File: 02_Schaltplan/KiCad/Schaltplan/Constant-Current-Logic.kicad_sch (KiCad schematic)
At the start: 42 parts, among them Q1 SI2318, U17 LMV321AUIDBVR, U18 LMV358MM, U19 INA826AIDRGT, U20 74HC595, U21 74HC595, U22 74AHC2G08

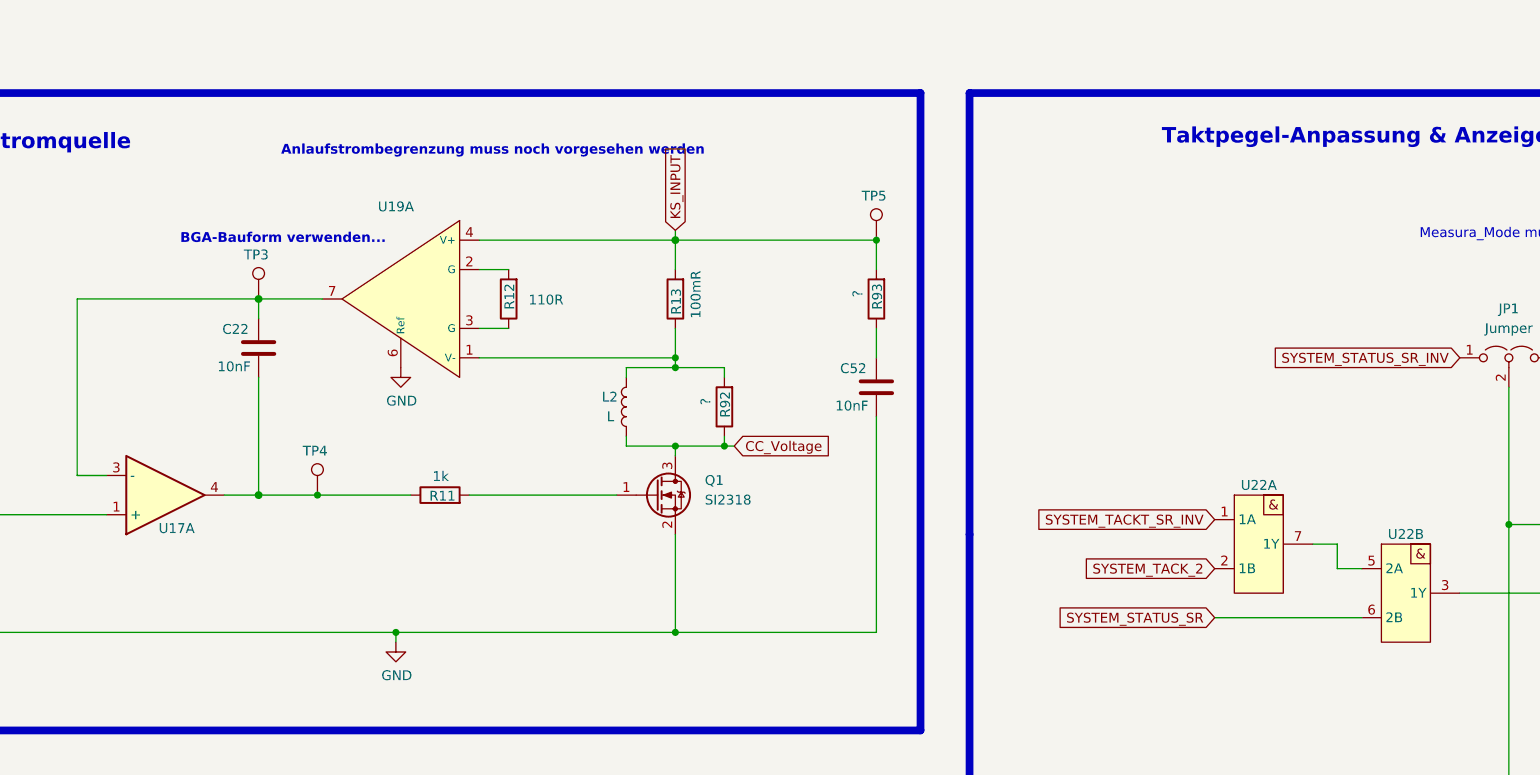
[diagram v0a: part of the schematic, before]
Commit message: Changes
constant-current
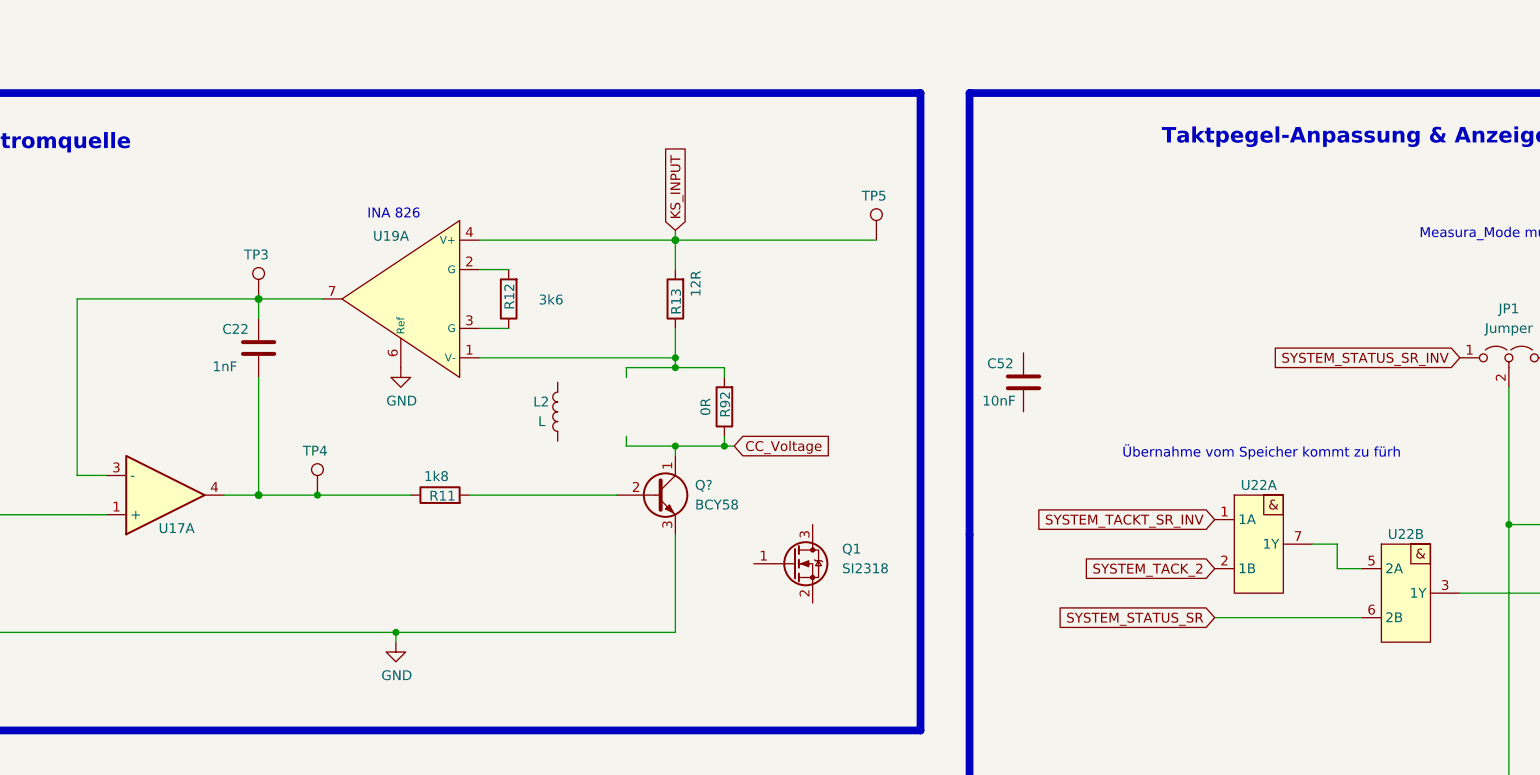
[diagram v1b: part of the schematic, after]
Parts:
- removed R93: ?, Resistor_SMD:R_0603_1608Metric_Pad0.98x0.95mm_HandSolder, symbol Device:R
- added Q?: BCY58, Package_TO_SOT_THT:TO-92_Inline, symbol Transistor_BJT:BC413
- C22: value 10nF -> 1nF
- R11: value 1k -> 1k8
- R12: value 110R -> 3k6
- R13: value 100mR -> 12R
- R92: value ? -> 0R
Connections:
- net CC_Voltage: now also Q?.1 (C); no longer L2.2, Q1.3 (D)
- net GND: now also Q?.3 (E); no longer C52.2, Q1.2 (S)
- net at R13.1, R92.2, U19.1 (V-): no longer L2.1
- net at R11.2: now also Q?.2 (B); no longer Q1.1 (G)
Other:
- note added: "INA 826"
- note added: "Übernahme vom Speicher kommt zu fürh"
- note removed: "Anlaufstrombegrenzung muss noch vorgesehen werden"
- note removed: "BGA-Bauform verwenden..."
- moved on the sheet: C52, L2, Q1
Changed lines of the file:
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@@
   (junction (at 171.45 86.36) (diameter 0.9144) (color 0 0 0 0))
   (junction (at 171.45 96.52) (diameter 0.9144) (color 0 0 0 0))
-  (junction (at 171.45 120.65) (diameter 0.9144) (color 0 0 0 0))
   (junction (at 174.625 243.84) (diameter 1.016) (color 0 0 0 0))
   (junction (at 174.625 265.43) (diameter 1.016) (color 0 0 0 0))
   (junction (at 177.8 96.52) (diameter 0.9144) (color 0 0 0 0))
-  (junction (at 197.485 69.85) (diameter 0.9144) (color 0 0 0 0))
   (junction (at 250.825 243.84) (diameter 0.9144) (color 0 0 0 0))
   (junction (at 250.825 264.16) (diameter 0.9144) (color 0 0 0 0))
@@
     (stroke (width 0) (type solid) (color 0 0 0 0))
   )
-  (wire (pts (xy 197.485 69.85) (xy 197.485 73.66))
-    (stroke (width 0) (type solid) (color 0 0 0 0))
-  )
-  (wire (pts (xy 197.485 81.28) (xy 197.485 85.09))
-    (stroke (width 0) (type solid) (color 0 0 0 0))
-  )
-  (wire (pts (xy 197.485 92.71) (xy 197.485 120.65))
-    (stroke (width 0) (type solid) (color 0 0 0 0))
-  )
-  (wire (pts (xy 197.485 120.65) (xy 171.45 120.65))
-    (stroke (width 0) (type solid) (color 0 0 0 0))
-  )
   (wire (pts (xy 241.3 118.745) (xy 260.35 118.745))
     (stroke (width 0) (type solid) (color 0 0 0 0))
@@
     (effects (font (size 2 2) (thickness 0.4) bold) (justify right bottom))
   )
-  (text "BGA-Bauform verwenden...\n" (at 133.985 70.485 180)
-    (effects (font (size 1.27 1.27) (thickness 0.254) bold) (justify right bottom))
-  )
-  (text "Anlaufstrombegrenzung muss noch vorgesehen werden\n"
-    (at 175.26 59.055 0)
-    (effects (font (size 1.27 1.27) (thickness 0.254) bold) (justify right bottom))
+  (text "INA 826\n" (at 138.43 67.31 180)
+    (effects (font (size 1.27 1.27)) (justify right bottom))
   )
   (text "Hysterese-Widerstand\n" (at 178.435 168.275 180)
+    (effects (font (size 1.27 1.27)) (justify right bottom))
+  )
+  (text "Übernahme vom Speicher kommt zu fürh\n\n" (at 265.43 100.33 180)
     (effects (font (size 1.27 1.27)) (justify right bottom))
   )
@@
     (pin "1")
   )
-  (symbol (lib_id "Device:L") (at 165.1 91.44 0) (mirror y) (unit 1)
-    (in_bom yes) (on_board yes)
-    (property "Reference" "L2" (id 0) (at 161.925 90.17 0)
+  (symbol (lib_id "Device:L") (at 156.21 92.075 0) (mirror y) (unit 1)
+    (in_bom yes) (on_board yes)
+    (property "Reference" "L2" (id 0) (at 153.035 90.805 0)
       (effects (font (size 1.27 1.27)) (justify right))
     )
-    (property "Value" "L" (id 1) (at 162.56 92.71 0)
+    (property "Value" "L" (id 1) (at 153.67 93.345 0)
       (effects (font (size 1.27 1.27)) (justify right))
     )
-    (property "Footprint" "Inductor_SMD:L_TDK_NLV32_3.2x2.5mm" (id 2) (at 165.1 91.44 0)
-      (effects (font (size 1.27 1.27)) hide)
-    )
-    (property "Datasheet" "~" (id 3) (at 165.1 91.44 0)
+    (property "Footprint" "Inductor_SMD:L_TDK_NLV32_3.2x2.5mm" (id 2) (at 156.21 92.075 0)
+      (effects (font (size 1.27 1.27)) hide)
+    )
+    (property "Datasheet" "~" (id 3) (at 156.21 92.075 0)
       (effects (font (size 1.27 1.27)) hide)
     )
@@
       (effects (font (size 1.27 1.27)) (justify left))
     )
-    (property "Value" "1k" (id 1) (at 142.119 100.457 90)
+    (property "Value" "1k8" (id 1) (at 142.119 100.457 90)
       (effects (font (size 1.27 1.27)) (justify left))
     )
@@
       (effects (font (size 1.27 1.27)) (justify left))
     )
-    (property "Value" "110R" (id 1) (at 156.972 77.591 0)
+    (property "Value" "3k6" (id 1) (at 156.972 77.591 0)
       (effects (font (size 1.27 1.27)) (justify left))
     )
@@
       (effects (font (size 1.27 1.27)) (justify left))
     )
-    (property "Value" "100mR" (id 1) (at 174.117 73.781 90)
+    (property "Value" "12R" (id 1) (at 174.117 73.781 90)
       (effects (font (size 1.27 1.27)) (justify left))
     )
@@
       (effects (font (size 1.27 1.27)) (justify left))
     )
-    (property "Value" "?" (id 1) (at 175.387 90.291 90)
+    (property "Value" "0R" (id 1) (at 175.387 90.291 90)
       (effects (font (size 1.27 1.27)) (justify left))
     )
@@
     (pin "2")
   )
-  (symbol (lib_id "Device:R") (at 197.485 77.47 180) (unit 1)
-    (in_bom yes) (on_board yes)
-    (property "Reference" "R93" (id 0) (at 197.6119 75.4444 90)
-      (effects (font (size 1.27 1.27)) (justify left))
-    )
-    (property "Value" "?" (id 1) (at 195.072 76.321 90)
-      (effects (font (size 1.27 1.27)) (justify left))
-    )
-    (property "Footprint" "Resistor_SMD:R_0603_1608Metric_Pad0.98x0.95mm_HandSolder" (id 2) (at 199.263 77.47 90)
-      (effects (font (size 1.27 1.27)) hide)
-    )
-    (property "Datasheet" "~" (id 3) (at 197.485 77.47 0)
-      (effects (font (size 1.27 1.27)) hide)
-    )
-    (property "BMK-Nr" "BS" (id 4) (at 197.485 77.47 0)
-      (effects (font (size 1.27 1.27)) hide)
-    )
-    (property "Mouser" "-" (id 4) (at 197.485 77.47 0)
-      (effects (font (size 1.27 1.27)) hide)
-    )
-    (pin "1")
-    (pin "2")
-  )
   (symbol (lib_name "Device:C_2") (lib_id "Device:C") (at 82.55 254 0) (unit 1)
     (in_bom yes) (on_board yes)
@@
       (effects (font (size 1.27 1.27)) (justify left))
     )
-    (property "Value" "10nF" (id 1) (at 112.141 86.239 0)
+    (property "Value" "1nF" (id 1) (at 111.506 86.239 0)
       (effects (font (size 1.27 1.27)) (justify left))
     )
@@
     (pin "2")
   )
-  (symbol (lib_name "Device:C_6") (lib_id "Device:C") (at 197.485 88.9 0) (unit 1)
-    (in_bom yes) (on_board yes)
-    (property "Reference" "C52" (id 0) (at 192.7861 86.4806 0)
-      (effects (font (size 1.27 1.27)) (justify left))
-    )
-    (property "Value" "10nF" (id 1) (at 192.151 91.319 0)
-      (effects (font (size 1.27 1.27)) (justify left))
-    )
-    (property "Footprint" "Capacitor_SMD:C_0603_1608Metric_Pad1.08x0.95mm_HandSolder" (id 2) (at 198.4502 92.71 0)
-      (effects (font (size 1.27 1.27)) hide)
-    )
-    (property "Datasheet" "~" (id 3) (at 197.485 88.9 0)
-      (effects (font (size 1.27 1.27)) hide)
-    )
-    (property "BMK-Nr" "BS" (id 4) (at 197.485 88.9 0)
+  (symbol (lib_name "Device:C_6") (lib_id "Device:C") (at 216.535 88.265 0) (unit 1)
+    (in_bom yes) (on_board yes)
+    (property "Reference" "C52" (id 0) (at 211.8361 85.8456 0)
+      (effects (font (size 1.27 1.27)) (justify left))
+    )
+    (property "Value" "10nF" (id 1) (at 211.201 90.684 0)
+      (effects (font (size 1.27 1.27)) (justify left))
+    )
+    (property "Footprint" "Capacitor_SMD:C_0603_1608Metric_Pad1.08x0.95mm_HandSolder" (id 2) (at 217.5002 92.075 0)
+      (effects (font (size 1.27 1.27)) hide)
+    )
+    (property "Datasheet" "~" (id 3) (at 216.535 88.265 0)
+      (effects (font (size 1.27 1.27)) hide)
+    )
+    (property "BMK-Nr" "BS" (id 4) (at 216.535 88.265 0)
       (effects (font (size 1.27 1.27)) hide)
     )
@@
     (pin "3")
   )
-  (symbol (lib_id "Transistor_FET:BSS123") (at 168.91 102.87 0) (unit 1)
-    (in_bom yes) (on_board yes)
-    (property "Reference" "Q1" (id 0) (at 175.26 100.965 0)
-      (effects (font (size 1.27 1.27)) (justify left))
-    )
-    (property "Value" "SI2318" (id 1) (at 175.26 103.505 0)
-      (effects (font (size 1.27 1.27)) (justify left))
-    )
-    (property "Footprint" "Package_TO_SOT_SMD:SOT-23" (id 2) (at 173.99 104.775 0)
+  (symbol (lib_id "Transistor_BJT:BC413") (at 168.91 102.87 0) (unit 1)
+    (in_bom yes) (on_board yes)
+    (property "Reference" "Q?" (id 0) (at 173.99 101.6 0)
+      (effects (font (size 1.27 1.27)) (justify left))
+    )
+    (property "Value" "BCY58" (id 1) (at 173.99 104.14 0)
+      (effects (font (size 1.27 1.27)) (justify left))
+    )
+    (property "Footprint" "Package_TO_SOT_THT:TO-92_Inline" (id 2) (at 173.99 104.775 0)
       (effects (font (size 1.27 1.27) italic) (justify left) hide)
     )
-    (property "Datasheet" "http://www.diodes.com/assets/Datasheets/ds30366.pdf" (id 3) (at 168.91 102.87 0)
-      (effects (font (size 1.27 1.27)) (justify left) hide)
-    )
-    (property "BMK-Nr" "08-8668" (id 4) (at 168.91 102.87 0)
-      (effects (font (size 1.27 1.27)) hide)
-    )
-    (property "Mouser" "781-SI2318CDS-T1-GE3" (id 4) (at 168.91 102.87 0)
+    (property "Datasheet" "http://www.cdil.com/datasheets/bc413_14_b_c.pdf" (id 3) (at 168.91 102.87 0)
+      (effects (font (size 1.27 1.27)) (justify left) hide)
+    )
+    (pin "1")
+    (pin "2")
+    (pin "3")
+  )
+  (symbol (lib_id "Transistor_FET:BSS123") (at 186.69 111.76 0) (unit 1)
+    (in_bom yes) (on_board yes)
+    (property "Reference" "Q1" (id 0) (at 193.04 109.855 0)
+      (effects (font (size 1.27 1.27)) (justify left))
+    )
+    (property "Value" "SI2318" (id 1) (at 193.04 112.395 0)
+      (effects (font (size 1.27 1.27)) (justify left))
+    )
+    (property "Footprint" "Package_TO_SOT_SMD:SOT-23" (id 2) (at 191.77 113.665 0)
+      (effects (font (size 1.27 1.27) italic) (justify left) hide)
+    )
+    (property "Datasheet" "http://www.diodes.com/assets/Datasheets/ds30366.pdf" (id 3) (at 186.69 111.76 0)
+      (effects (font (size 1.27 1.27)) (justify left) hide)
+    )
+    (property "BMK-Nr" "08-8668" (id 4) (at 186.69 111.76 0)
+      (effects (font (size 1.27 1.27)) hide)
+    )
+    (property "Mouser" "781-SI2318CDS-T1-GE3" (id 4) (at 186.69 111.76 0)
       (effects (font (size 1.27 1.27)) hide)
     )
@@
   (symbol (lib_id "Kabeltester:INA826AIDRGT") (at 137.795 77.47 0) (mirror y) (unit 1)
     (in_bom yes) (on_board yes)
-    (property "Reference" "U19" (id 0) (at 135.255 65.5256 0))
+    (property "Reference" "U19" (id 0) (at 134.62 69.3356 0))
     (property "Value" "INA826AIDRGT" (id 1) (at 134.62 67.672 0)
       (effects (font (size 1.27 1.27)) hide)

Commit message: Changes
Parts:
- removed C52: 10nF, Capacitor_SMD:C_0603_1608Metric_Pad1.08x0.95mm_HandSolder, symbol Device:C
- removed Q?: BCY58, Package_TO_SOT_THT:TO-92_Inline, symbol Transistor_BJT:BC413
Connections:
- net CC_Voltage: now also L2.2, Q1.3 (D)
- net GND: now also Q1.2 (S)
- net at R11.2: now also Q1.1 (G)
- net at R13.1, R92.2, U19.1 (V-): now also L2.1
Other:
- note added: "Übernahme vom Speicher kommt zu fürh Takt2 inv"
- note removed: "Übernahme vom Speicher kommt zu fürh"
- moved on the sheet: L2, Q1
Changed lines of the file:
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@@
     (stroke (width 1) (type solid) (color 255 0 0 1))
+  )
+  (polyline (pts (xy 167.64 88.9) (xy 161.925 94.615))
+    (stroke (width 0.3) (type solid) (color 255 0 0 1))
+  )
+  (polyline (pts (xy 167.64 94.615) (xy 161.925 88.9))
+    (stroke (width 0.3) (type solid) (color 255 0 0 1))
   )
   (polyline (pts (xy 203.2 50.8) (xy 203.2 133.35))
@@
     (effects (font (size 1.27 1.27)) (justify right bottom))
   )
-  (text "Übernahme vom Speicher kommt zu fürh\n\n" (at 265.43 100.33 180)
+  (text "Übernahme vom Speicher kommt zu fürh\n\nTakt2 inv\n" (at 265.43 100.33 180)
     (effects (font (size 1.27 1.27)) (justify right bottom))
   )
@@
     (pin "1")
   )
-  (symbol (lib_id "Device:L") (at 156.21 92.075 0) (mirror y) (unit 1)
-    (in_bom yes) (on_board yes)
-    (property "Reference" "L2" (id 0) (at 153.035 90.805 0)
+  (symbol (lib_id "Device:L") (at 165.1 91.44 0) (mirror y) (unit 1)
+    (in_bom yes) (on_board yes)
+    (property "Reference" "L2" (id 0) (at 161.925 90.17 0)
       (effects (font (size 1.27 1.27)) (justify right))
     )
-    (property "Value" "L" (id 1) (at 153.67 93.345 0)
+    (property "Value" "L" (id 1) (at 162.56 92.71 0)
       (effects (font (size 1.27 1.27)) (justify right))
     )
-    (property "Footprint" "Inductor_SMD:L_TDK_NLV32_3.2x2.5mm" (id 2) (at 156.21 92.075 0)
-      (effects (font (size 1.27 1.27)) hide)
-    )
-    (property "Datasheet" "~" (id 3) (at 156.21 92.075 0)
+    (property "Footprint" "Inductor_SMD:L_TDK_NLV32_3.2x2.5mm" (id 2) (at 165.1 91.44 0)
+      (effects (font (size 1.27 1.27)) hide)
+    )
+    (property "Datasheet" "~" (id 3) (at 165.1 91.44 0)
       (effects (font (size 1.27 1.27)) hide)
     )
@@
     )
     (property "BMK-Nr" "BS" (id 4) (at 184.15 254 0)
-      (effects (font (size 1.27 1.27)) hide)
-    )
-    (pin "1")
-    (pin "2")
-  )
-  (symbol (lib_name "Device:C_6") (lib_id "Device:C") (at 216.535 88.265 0) (unit 1)
-    (in_bom yes) (on_board yes)
-    (property "Reference" "C52" (id 0) (at 211.8361 85.8456 0)
-      (effects (font (size 1.27 1.27)) (justify left))
-    )
-    (property "Value" "10nF" (id 1) (at 211.201 90.684 0)
-      (effects (font (size 1.27 1.27)) (justify left))
-    )
-    (property "Footprint" "Capacitor_SMD:C_0603_1608Metric_Pad1.08x0.95mm_HandSolder" (id 2) (at 217.5002 92.075 0)
-      (effects (font (size 1.27 1.27)) hide)
-    )
-    (property "Datasheet" "~" (id 3) (at 216.535 88.265 0)
-      (effects (font (size 1.27 1.27)) hide)
-    )
-    (property "BMK-Nr" "BS" (id 4) (at 216.535 88.265 0)
       (effects (font (size 1.27 1.27)) hide)
     )
@@
     (pin "3")
   )
-  (symbol (lib_id "Transistor_BJT:BC413") (at 168.91 102.87 0) (unit 1)
-    (in_bom yes) (on_board yes)
-    (property "Reference" "Q?" (id 0) (at 173.99 101.6 0)
-      (effects (font (size 1.27 1.27)) (justify left))
-    )
-    (property "Value" "BCY58" (id 1) (at 173.99 104.14 0)
-      (effects (font (size 1.27 1.27)) (justify left))
-    )
-    (property "Footprint" "Package_TO_SOT_THT:TO-92_Inline" (id 2) (at 173.99 104.775 0)
+  (symbol (lib_id "Transistor_FET:BSS123") (at 168.91 102.87 0) (unit 1)
+    (in_bom yes) (on_board yes)
+    (property "Reference" "Q1" (id 0) (at 175.26 100.965 0)
+      (effects (font (size 1.27 1.27)) (justify left))
+    )
+    (property "Value" "SI2318" (id 1) (at 175.26 103.505 0)
+      (effects (font (size 1.27 1.27)) (justify left))
+    )
+    (property "Footprint" "Package_TO_SOT_SMD:SOT-23" (id 2) (at 173.99 104.775 0)
       (effects (font (size 1.27 1.27) italic) (justify left) hide)
     )
-    (property "Datasheet" "http://www.cdil.com/datasheets/bc413_14_b_c.pdf" (id 3) (at 168.91 102.87 0)
-      (effects (font (size 1.27 1.27)) (justify left) hide)
-    )
-    (pin "1")
-    (pin "2")
-    (pin "3")
-  )
-  (symbol (lib_id "Transistor_FET:BSS123") (at 186.69 111.76 0) (unit 1)
-    (in_bom yes) (on_board yes)
-    (property "Reference" "Q1" (id 0) (at 193.04 109.855 0)
-      (effects (font (size 1.27 1.27)) (justify left))
-    )
-    (property "Value" "SI2318" (id 1) (at 193.04 112.395 0)
-      (effects (font (size 1.27 1.27)) (justify left))
-    )
-    (property "Footprint" "Package_TO_SOT_SMD:SOT-23" (id 2) (at 191.77 113.665 0)
-      (effects (font (size 1.27 1.27) italic) (justify left) hide)
-    )
-    (property "Datasheet" "http://www.diodes.com/assets/Datasheets/ds30366.pdf" (id 3) (at 186.69 111.76 0)
-      (effects (font (size 1.27 1.27)) (justify left) hide)
-    )
-    (property "BMK-Nr" "08-8668" (id 4) (at 186.69 111.76 0)
-      (effects (font (size 1.27 1.27)) hide)
-    )
-    (property "Mouser" "781-SI2318CDS-T1-GE3" (id 4) (at 186.69 111.76 0)
-      (effects (font (size 1.27 1.27)) hide)
-    )
+    (property "Datasheet" "http://www.diodes.com/assets/Datasheets/ds30366.pdf" (id 3) (at 168.91 102.87 0)
+      (effects (font (size 1.27 1.27)) (justify left) hide)
+    )
+    (property "BMK-Nr" "08-8668" (id 4) (at 168.91 102.87 0)
+      (effects (font (size 1.27 1.27)) hide)
+    )
+    (property "Mouser" "781-SI2318CDS-T1-GE3" (id 4) (at 168.91 102.87 0)
+      (effects (font (size 1.27 1.27)) hide)
+    )
